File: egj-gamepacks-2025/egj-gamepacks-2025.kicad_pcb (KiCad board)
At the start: 2 copper layers, 52.3 x 64 mm, 81 parts, among them J1 USB_B_Micro, J2 Conn_01x03_Pin, J5 GameBoy_GamePak_AGB-002, SW1 SW_Push, SW2 SW_Push, U1 W25Q128JVS, U10 SP3012-06UTG, U11 VL6180XV0NR_1, U12 TXS0108EPW, U13 LD1117S18TR_SOT223, U14 BNO055, U15 SP3012-06UTG, U2 DNF, U3 NCP1117-3.3_SOT223, U4 RP2350_80QFN, U5 USBLC6-2P6, U6 SP3012-06UTG, U7 SP3012-06UTG, U8 SP3012-06UTG, U9 SP3012-06UTG, Y1 ABM8-272-T3

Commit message: UPDATE: sync local schematic and board work
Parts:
- removed C23: 100u, Capacitor_SMD:C_0805_2012Metric
- removed D1: BAT54CW, Package_TO_SOT_SMD:SOT-323_SC-70
- removed J2: Conn_01x03_Pin, Connector_PinHeader_2.54mm:PinHeader_1x03_P2.54mm_Horizontal
- removed U15: SP3012-06UTG, Package_DFN_QFN:DFN-14_1.35x3.5mm_P0.5mm
- added J3: SM03B-SRSS-TB, Connector_JST:JST_SH_SM03B-SRSS-TB_1x03-1MP_P1.00mm_Horizontal, F.Cu at (251.0, 109.0)
- added TP1: TestPoint, TestPoint:TestPoint_Keystone_5015_Micro_Mini, F.Cu at (261.0, 77.0)
- added TP2: TestPoint, TestPoint:TestPoint_Keystone_5015_Micro_Mini, F.Cu at (254.0, 75.0)
- added TP8: TestPoint, TestPoint:TestPoint_Keystone_5015_Micro_Mini, F.Cu at (246.0, 85.0)
- U13: value LD1117S18TR_SOT223 -> AP7361C-28E
- moved C9 140.2 mm to (273.0, 87.0), turned to 0 degrees
- moved C11 139.9 mm to (273.0, 91.0), turned to 0 degrees
- moved C8 139.9 mm to (273.0, 92.0), turned to 0 degrees
- moved R4 139.5 mm to (263.0, 93.0), turned to 0 degrees
- moved R19 133.6 mm to (273.0, 89.0), turned to 180 degrees
- moved R5 132.5 mm to (256.0, 106.0), turned to 0 degrees
- moved U1 131.5 mm to (256.0, 95.0)
- moved U2 131.5 mm to (256.0, 102.0)
- moved C12 129.8 mm to (263.0, 95.0), turned to 0 degrees
- moved R2 129.0 mm to (249.0, 105.0)
- moved SW1 128.6 mm to (244.0, 112.0)
- moved C3 127.8 mm to (248.0, 66.0)
- moved L1 127.4 mm to (263.0, 100.0)
- moved R10 126.7 mm to (273.0, 85.0), turned to 0 degrees
- moved U12 125.5 mm to (269.0, 97.0), turned to 180 degrees
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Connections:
- net /RP2350/+1V1 renamed +1V1
- C24 pad 1: +1V8 -> +2V8
- C26 pad 1: +1V8 -> +2V8
- C28 pad 1: +1V8 -> +2V8
- C29 pad 1: +1V8 -> +2V8
- C6 pad 1: +3V3_USB -> +3V3
- R10 pad 1: /Power/USB.USB_D_C+ -> /RP2350/USB_D+
- R11 pad 1: /Power/USB.USB_D_C- -> /RP2350/USB_D-
- R13 pad 1: +1V8 -> +2V8
- R14 pad 1: +1V8 -> +2V8
- R17 pad 1: +1V8 -> +2V8
- R18 pad 1: +1V8 -> +2V8
- U10 pad 1: /GBA_Connector/GBA_ADD13 -> unconnected-(U10-Pad1)
- U10 pad 11: /GBA_Connector/GBA_DATA0 -> /GBA_Connector/GBA_SIG.N_CS
- U10 pad 12: /GBA_Connector/GBA_ADD15 -> /GBA_Connector/GBA_SIG.N_RD
- U10 pad 13: /GBA_Connector/GBA_ADD14 -> /GBA_Connector/GBA_SIG.N_WR
- U10 pad 14: /GBA_Connector/GBA_ADD13 -> /GBA_Connector/GBA_SIG.PHI
- U10 pad 2: /GBA_Connector/GBA_ADD14 -> unconnected-(U10-Pad2)
- U10 pad 3: /GBA_Connector/GBA_ADD15 -> unconnected-(U10-Pad3)
- U10 pad 4: /GBA_Connector/GBA_DATA0 -> unconnected-(U10-Pad4)
- U10 pad 5: GND -> unconnected-(U10-Pad5)
- U10 pad 6: /GBA_Connector/GBA_DATA1 -> unconnected-(U10-Pad6)
- U10 pad 7: /GBA_Connector/GBA_DATA2 -> unconnected-(U10-Pad7)
- U10 pad 8: /GBA_Connector/GBA_DATA2 -> /GBA_Connector/GBA_SIG.IRQ
- U10 pad 9: /GBA_Connector/GBA_DATA1 -> /GBA_Connector/GBA_SIG.N_CS2
- U11 pad 10: +1V8 -> +2V8
- U11 pad 8: +1V8 -> +2V8
- U12 pad 2: +1V8 -> +2V8
- U13 pad 1: GND -> +3V3
- U13 pad 2: +1V8 -> GND
- U13 pad 3: +3V3 -> +2V8
- U3 pad 2: +3V3_USB -> +3V3
- U4 pad 1: /GBA_Connector/GBA_ADD0 -> /GBA_Connector/GBA_DATA4
- U4 pad 11: /GBA_Connector/GBA_ADD8 -> /GBA_Connector/GBA_ADD4
- U4 pad 12: /GBA_Connector/GBA_ADD9 -> /GBA_Connector/GBA_ADD5
- U4 pad 13: /GBA_Connector/GBA_ADD10 -> /GBA_Connector/GBA_ADD6
- U4 pad 14: /GBA_Connector/GBA_ADD11 -> /GBA_Connector/GBA_ADD7
- U4 pad 16: /GBA_Connector/GBA_ADD12 -> /GBA_Connector/GBA_ADD8
- U4 pad 17: /GBA_Connector/GBA_ADD13 -> /GBA_Connector/GBA_ADD9
- U4 pad 18: /GBA_Connector/GBA_ADD14 -> /GBA_Connector/GBA_ADD10
- U4 pad 19: /GBA_Connector/GBA_ADD15 -> /GBA_Connector/GBA_ADD11
- U4 pad 2: /GBA_Connector/GBA_ADD1 -> /GBA_Connector/GBA_DATA5
- U4 pad 20: /GBA_Connector/GBA_DATA0 -> /GBA_Connector/GBA_ADD12
- U4 pad 21: /GBA_Connector/GBA_DATA1 -> /GBA_Connector/GBA_ADD13
- U4 pad 22: /GBA_Connector/GBA_DATA2 -> /GBA_Connector/GBA_ADD14
- U4 pad 23: /GBA_Connector/GBA_DATA3 -> /GBA_Connector/GBA_ADD15
- U4 pad 25: /GBA_Connector/GBA_DATA4 -> /GBA_Connector/GBA_SIG.PHI
- U4 pad 26: /GBA_Connector/GBA_DATA5 -> /GBA_Connector/GBA_SIG.N_WR
- U4 pad 27: /GBA_Connector/GBA_DATA6 -> /GBA_Connector/GBA_SIG.N_RD
- U4 pad 28: /GBA_Connector/GBA_DATA7 -> /GBA_Connector/GBA_SIG.N_CS
- U4 pad 3: /GBA_Connector/GBA_ADD2 -> /GBA_Connector/GBA_DATA6
- U4 pad 4: /GBA_Connector/GBA_ADD3 -> /GBA_Connector/GBA_DATA7
- U4 pad 58: +3V3_USB -> unconnected-(U4-GPIO47_ADC7-Pad58)
- U4 pad 6: /GBA_Connector/GBA_ADD4 -> /GBA_Connector/GBA_ADD0
- U4 pad 7: /GBA_Connector/GBA_ADD5 -> /GBA_Connector/GBA_ADD1
- U4 pad 77: /GBA_Connector/GBA_SIG.PHI -> /GBA_Connector/GBA_DATA0
- U4 pad 78: /GBA_Connector/GBA_SIG.N_WR -> /GBA_Connector/GBA_DATA1
- U4 pad 79: /GBA_Connector/GBA_SIG.N_RD -> /GBA_Connector/GBA_DATA2
- U4 pad 8: /GBA_Connector/GBA_ADD6 -> /GBA_Connector/GBA_ADD2
- U4 pad 80: /GBA_Connector/GBA_SIG.N_CS -> /GBA_Connector/GBA_DATA3
- U4 pad 9: /GBA_Connector/GBA_ADD7 -> /GBA_Connector/GBA_ADD3
- U5 pad 2: unconnected-(U5-GND-Pad2) -> GND
- U5 pad 4: /Power/USB.USB_D_C- -> /RP2350/USB_D-
- U5 pad 5: GND -> VBUS
- U5 pad 6: /Power/USB.USB_D_C+ -> /RP2350/USB_D+
- U6 pad 1: /GBA_Connector/GBA_DATA3 -> unconnected-(U6-Pad1)
- U6 pad 11: /GBA_Connector/GBA_DATA6 -> /GBA_Connector/GBA_DATA3
- U6 pad 12: /GBA_Connector/GBA_DATA5 -> /GBA_Connector/GBA_DATA2
- U6 pad 13: /GBA_Connector/GBA_DATA4 -> /GBA_Connector/GBA_DATA1
- U6 pad 14: /GBA_Connector/GBA_DATA3 -> /GBA_Connector/GBA_DATA0
- U6 pad 2: /GBA_Connector/GBA_DATA4 -> unconnected-(U6-Pad2)
- U6 pad 3: /GBA_Connector/GBA_DATA5 -> unconnected-(U6-Pad3)
- U6 pad 4: /GBA_Connector/GBA_DATA6 -> unconnected-(U6-Pad4)
- U6 pad 5: GND -> unconnected-(U6-Pad5)
- U6 pad 6: /GBA_Connector/GBA_DATA7 -> unconnected-(U6-Pad6)
- U6 pad 7: /GBA_Connector/GBA_SIG.N_CS2 -> unconnected-(U6-Pad7)
- U6 pad 8: /GBA_Connector/GBA_SIG.N_CS2 -> /GBA_Connector/GBA_DATA5
- U6 pad 9: /GBA_Connector/GBA_DATA7 -> /GBA_Connector/GBA_DATA4
- U7 pad 1: /GBA_Connector/GBA_SIG.PHI -> unconnected-(U7-Pad1)
- U7 pad 11: /GBA_Connector/GBA_SIG.N_CS -> /GBA_Connector/GBA_ADD1
- U7 pad 12: /GBA_Connector/GBA_SIG.N_RD -> /GBA_Connector/GBA_ADD0
- U7 pad 13: /GBA_Connector/GBA_SIG.N_WR -> /GBA_Connector/GBA_DATA7
- U7 pad 14: /GBA_Connector/GBA_SIG.PHI -> /GBA_Connector/GBA_DATA6
- U7 pad 2: /GBA_Connector/GBA_SIG.N_WR -> unconnected-(U7-Pad2)
- U7 pad 3: /GBA_Connector/GBA_SIG.N_RD -> unconnected-(U7-Pad3)
- U7 pad 4: /GBA_Connector/GBA_SIG.N_CS -> unconnected-(U7-Pad4)
- U7 pad 5: GND -> unconnected-(U7-Pad5)
- U7 pad 6: /GBA_Connector/GBA_ADD0 -> unconnected-(U7-Pad6)
- U7 pad 7: /GBA_Connector/GBA_ADD1 -> unconnected-(U7-Pad7)
- U7 pad 8: /GBA_Connector/GBA_ADD1 -> /GBA_Connector/GBA_ADD3
- U7 pad 9: /GBA_Connector/GBA_ADD0 -> /GBA_Connector/GBA_ADD2
- U8 pad 1: /GBA_Connector/GBA_ADD2 -> unconnected-(U8-Pad1)
- U8 pad 11: /GBA_Connector/GBA_ADD4 -> /GBA_Connector/GBA_ADD7
- U8 pad 12: /GBA_Connector/GBA_ADD3 -> /GBA_Connector/GBA_ADD6
- U8 pad 13: /GBA_Connector/GBA_ADD2 -> /GBA_Connector/GBA_ADD5
- U8 pad 14: /GBA_Connector/GBA_ADD2 -> /GBA_Connector/GBA_ADD4
- U8 pad 2: /GBA_Connector/GBA_ADD2 -> unconnected-(U8-Pad2)
- U8 pad 3: /GBA_Connector/GBA_ADD3 -> unconnected-(U8-Pad3)
- U8 pad 4: /GBA_Connector/GBA_ADD4 -> unconnected-(U8-Pad4)
- U8 pad 5: GND -> unconnected-(U8-Pad5)
- U8 pad 6: /GBA_Connector/GBA_ADD5 -> unconnected-(U8-Pad6)
- U8 pad 7: /GBA_Connector/GBA_ADD6 -> unconnected-(U8-Pad7)
- U8 pad 8: /GBA_Connector/GBA_ADD6 -> /GBA_Connector/GBA_ADD9
- U8 pad 9: /GBA_Connector/GBA_ADD5 -> /GBA_Connector/GBA_ADD8
- U9 pad 1: /GBA_Connector/GBA_ADD7 -> unconnected-(U9-Pad1)
- U9 pad 11: /GBA_Connector/GBA_ADD10 -> /GBA_Connector/GBA_ADD13
- U9 pad 12: /GBA_Connector/GBA_ADD9 -> /GBA_Connector/GBA_ADD12
- U9 pad 13: /GBA_Connector/GBA_ADD8 -> /GBA_Connector/GBA_ADD11
- U9 pad 14: /GBA_Connector/GBA_ADD7 -> /GBA_Connector/GBA_ADD10
- U9 pad 2: /GBA_Connector/GBA_ADD8 -> unconnected-(U9-Pad2)
- U9 pad 3: /GBA_Connector/GBA_ADD9 -> unconnected-(U9-Pad3)
- U9 pad 4: /GBA_Connector/GBA_ADD10 -> unconnected-(U9-Pad4)
- U9 pad 5: GND -> unconnected-(U9-Pad5)
- U9 pad 6: /GBA_Connector/GBA_ADD11 -> unconnected-(U9-Pad6)
- U9 pad 7: /GBA_Connector/GBA_ADD12 -> unconnected-(U9-Pad7)
- U9 pad 8: /GBA_Connector/GBA_ADD12 -> /GBA_Connector/GBA_ADD15
- U9 pad 9: /GBA_Connector/GBA_ADD11 -> /GBA_Connector/GBA_ADD14
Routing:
- net +3V3: track 55.3 -> 0.00 mm
- net /GBA_Connector/GBA_ADD0: track 0.00 -> 32.9 mm
- net /GBA_Connector/GBA_ADD1: track 0.00 -> 31.3 mm
- net /GBA_Connector/GBA_ADD2: track 0.00 -> 29.8 mm
- net /GBA_Connector/GBA_ADD3: track 0.00 -> 28.3 mm
- net /GBA_Connector/GBA_ADD4: track 0.00 -> 26.7 mm
- net /GBA_Connector/GBA_ADD5: track 0.00 -> 25.2 mm
- net /GBA_Connector/GBA_ADD6: track 0.00 -> 23.6 mm
- net /GBA_Connector/GBA_ADD7: track 0.00 -> 22.1 mm
- net VBUS: track 21.7 -> 0.00 mm
- net /GBA_Connector/GBA_ADD8: track 0.00 -> 20.6 mm
- net /GBA_Connector/GBA_ADD9: track 0.00 -> 19.0 mm
- net +3V3_USB: track 17.0 -> 0.00 mm
- net +1V8: track 8.68 -> 0.00 mm
- net +3V3_GBA: track 1.87 -> 0.00 mm
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- removed copper zone on B.Cu, net (none)
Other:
- outline, holes or cut-outs redrawn

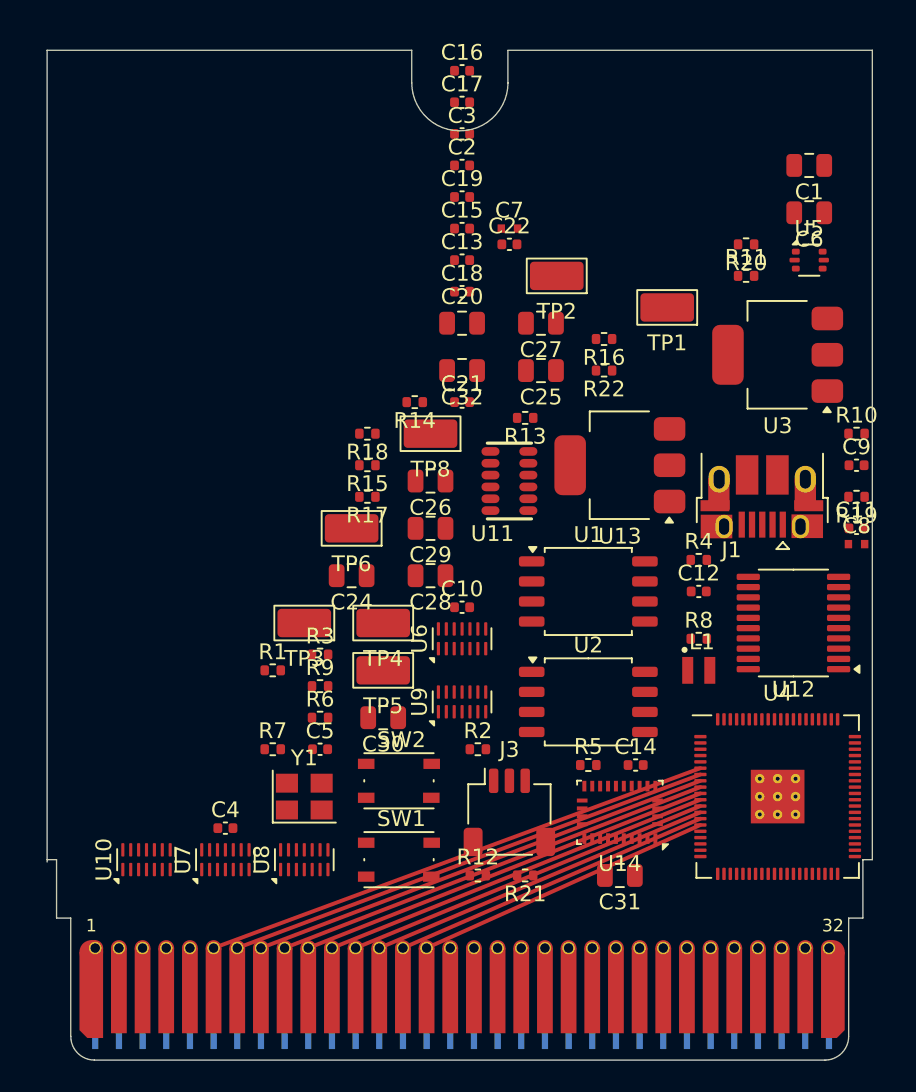
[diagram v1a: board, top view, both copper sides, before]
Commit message: ADD: board placement and full two-layer routing with JLCPCB design rules
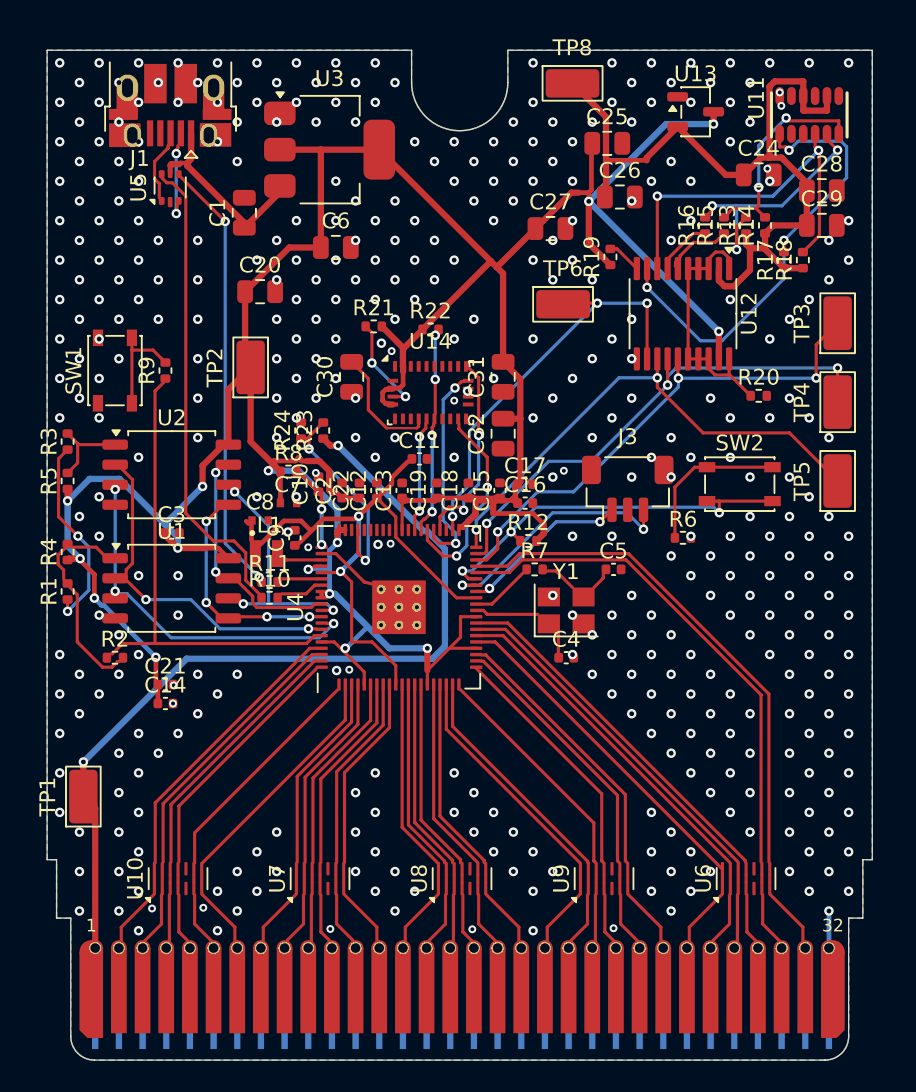
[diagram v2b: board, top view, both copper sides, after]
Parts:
- added R23: 100k, Resistor_SMD:R_0402_1005Metric, F.Cu at (239.2, 84.8)
- added R24: 100k, Resistor_SMD:R_0402_1005Metric, F.Cu at (237.8, 84.8)
- J3: value SM03B-SRSS-TB -> BM03B-SRSS-TB; footprint Connector_JST:JST_SH_SM03B-SRSS-TB_1x03-1MP_P1.00mm_Horizontal -> Connector_JST:JST_SH_BM03B-SRSS-TB_1x03-1MP_P1.00mm_Vertical
- SW1, SW2: value SW_Push -> PTS810SJG250SMTRLFS; footprint Button_Switch_SMD:SW_Push_1P1T_NO_Vertical_Wuerth_434133025816 -> Button_Switch_SMD:SW_SPST_PTS810
- U1: value W25Q128JVS -> W25Q128JVSIQ
- U10, U6, U7, U8, U9: value SP3012-06UTG -> TPD6E05U06RVZR
- U11: value VL6180XV0NR_1 -> VL6180V1NR/1
- U13: value AP7361C-28E -> XC6206P282MR; footprint Package_TO_SOT_SMD:SOT-223-3_TabPin2 -> Package_TO_SOT_SMD:SOT-23-3
- moved TP1 48.3 mm to (224.0, 108.0), turned to 90 degrees
- moved J1 45.0 mm to (229.5, 64.2)
- moved U5 40.8 mm to (229.5, 69.4), turned to 90 degrees
- moved R4 40.0 mm to (223.0, 92.5), turned to 90 degrees
- moved TP3 38.8 mm to (271.8, 78.0), turned to 90 degrees
- moved R10 38.6 mm to (235.8, 95.4)
- moved C8 37.8 mm to (235.2, 90.5)
- moved R5 37.6 mm to (223.0, 88.0), turned to 90 degrees
- moved C24 36.2 mm to (266.8, 68.6), turned to 0 degrees
- moved R21 36.1 mm to (242.4, 78.2), turned to 0 degrees
- moved C1 35.9 mm to (234.2, 71.0), turned to 90 degrees
- moved C9 35.9 mm to (237.4, 91.6), turned to 90 degrees
- moved R11 35.9 mm to (235.8, 94.4)
- moved SW1 35.8 mm to (226.0, 81.0), turned to 90 degrees
- moved C28 34.8 mm to (270.8, 69.6), turned to 0 degrees
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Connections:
- R22 pad 1: /RP2350/BNO055_UART.RESET -> +3V3
- R22 pad 2: +3V3 -> /RP2350/BNO055_UART.RESET
- U10 pad 1: unconnected-(U10-Pad1) -> /GBA_Connector/GBA_SIG.PHI
- U10 pad 2: unconnected-(U10-Pad2) -> /GBA_Connector/GBA_SIG.N_WR
- U10 pad 3: unconnected-(U10-Pad3) -> /GBA_Connector/GBA_SIG.N_RD
- U10 pad 4: unconnected-(U10-Pad4) -> /GBA_Connector/GBA_SIG.N_CS
- U10 pad 5: unconnected-(U10-Pad5) -> GND
- U10 pad 6: unconnected-(U10-Pad6) -> /GBA_Connector/GBA_ADD0
- U10 pad 7: unconnected-(U10-Pad7) -> /GBA_Connector/GBA_ADD1
- U10 pad 8: /GBA_Connector/GBA_SIG.IRQ -> /GBA_Connector/GBA_ADD1
- U10 pad 9: /GBA_Connector/GBA_SIG.N_CS2 -> /GBA_Connector/GBA_ADD0
- U13 pad 1: +3V3 -> GND
- U13 pad 2: GND -> +2V8
- U13 pad 3: +2V8 -> +3V3
- U14 pad 11: +3V3 -> /RP2350/BNO055_UART.RESET
- U4 pad 1: /GBA_Connector/GBA_DATA4 -> /GBA_Connector/GBA_ADD0
- U4 pad 11: /GBA_Connector/GBA_ADD4 -> /GBA_Connector/GBA_ADD8
- U4 pad 12: /GBA_Connector/GBA_ADD5 -> /GBA_Connector/GBA_ADD9
- U4 pad 13: /GBA_Connector/GBA_ADD6 -> /GBA_Connector/GBA_ADD10
- U4 pad 14: /GBA_Connector/GBA_ADD7 -> /GBA_Connector/GBA_ADD11
- U4 pad 16: /GBA_Connector/GBA_ADD8 -> /GBA_Connector/GBA_ADD12
- U4 pad 17: /GBA_Connector/GBA_ADD9 -> /GBA_Connector/GBA_ADD13
- U4 pad 18: /GBA_Connector/GBA_ADD10 -> /GBA_Connector/GBA_ADD14
- U4 pad 19: /GBA_Connector/GBA_ADD11 -> /GBA_Connector/GBA_ADD15
- U4 pad 2: /GBA_Connector/GBA_DATA5 -> /GBA_Connector/GBA_ADD1
- U4 pad 20: /GBA_Connector/GBA_ADD12 -> /GBA_Connector/GBA_DATA0
- U4 pad 21: /GBA_Connector/GBA_ADD13 -> /GBA_Connector/GBA_DATA1
- U4 pad 22: /GBA_Connector/GBA_ADD14 -> /GBA_Connector/GBA_DATA2
- U4 pad 23: /GBA_Connector/GBA_ADD15 -> /GBA_Connector/GBA_DATA3
- U4 pad 25: /GBA_Connector/GBA_SIG.PHI -> /GBA_Connector/GBA_DATA4
- U4 pad 26: /GBA_Connector/GBA_SIG.N_WR -> /GBA_Connector/GBA_DATA5
- U4 pad 27: /GBA_Connector/GBA_SIG.N_RD -> /GBA_Connector/GBA_DATA6
- U4 pad 28: /GBA_Connector/GBA_SIG.N_CS -> /GBA_Connector/GBA_DATA7
- U4 pad 3: /GBA_Connector/GBA_DATA6 -> /GBA_Connector/GBA_ADD2
- U4 pad 4: /GBA_Connector/GBA_DATA7 -> /GBA_Connector/GBA_ADD3
- U4 pad 57: +3V3_GBA -> Net-(U4-GPIO46_ADC6)
- U4 pad 6: /GBA_Connector/GBA_ADD0 -> /GBA_Connector/GBA_ADD4
- U4 pad 7: /GBA_Connector/GBA_ADD1 -> /GBA_Connector/GBA_ADD5
- U4 pad 77: /GBA_Connector/GBA_DATA0 -> /GBA_Connector/GBA_SIG.PHI
- U4 pad 78: /GBA_Connector/GBA_DATA1 -> /GBA_Connector/GBA_SIG.N_WR
- U4 pad 79: /GBA_Connector/GBA_DATA2 -> /GBA_Connector/GBA_SIG.N_RD
- U4 pad 8: /GBA_Connector/GBA_ADD2 -> /GBA_Connector/GBA_ADD6
- U4 pad 80: /GBA_Connector/GBA_DATA3 -> /GBA_Connector/GBA_SIG.N_CS
- U4 pad 9: /GBA_Connector/GBA_ADD3 -> /GBA_Connector/GBA_ADD7
- U6 pad 1: unconnected-(U6-Pad1) -> /GBA_Connector/GBA_DATA4
- U6 pad 11: /GBA_Connector/GBA_DATA3 -> /GBA_Connector/GBA_DATA7
- U6 pad 12: /GBA_Connector/GBA_DATA2 -> /GBA_Connector/GBA_DATA6
- U6 pad 13: /GBA_Connector/GBA_DATA1 -> /GBA_Connector/GBA_DATA5
- U6 pad 14: /GBA_Connector/GBA_DATA0 -> /GBA_Connector/GBA_DATA4
- U6 pad 2: unconnected-(U6-Pad2) -> /GBA_Connector/GBA_DATA5
- U6 pad 3: unconnected-(U6-Pad3) -> /GBA_Connector/GBA_DATA6
- U6 pad 4: unconnected-(U6-Pad4) -> /GBA_Connector/GBA_DATA7
- U6 pad 5: unconnected-(U6-Pad5) -> GND
- U6 pad 6: unconnected-(U6-Pad6) -> /GBA_Connector/GBA_SIG.N_CS2
- U6 pad 7: unconnected-(U6-Pad7) -> /GBA_Connector/GBA_SIG.IRQ
- U6 pad 8: /GBA_Connector/GBA_DATA5 -> /GBA_Connector/GBA_SIG.IRQ
- U6 pad 9: /GBA_Connector/GBA_DATA4 -> /GBA_Connector/GBA_SIG.N_CS2
- U7 pad 1: unconnected-(U7-Pad1) -> /GBA_Connector/GBA_ADD2
- U7 pad 11: /GBA_Connector/GBA_ADD1 -> /GBA_Connector/GBA_ADD5
- U7 pad 12: /GBA_Connector/GBA_ADD0 -> /GBA_Connector/GBA_ADD4
- U7 pad 13: /GBA_Connector/GBA_DATA7 -> /GBA_Connector/GBA_ADD3
- U7 pad 14: /GBA_Connector/GBA_DATA6 -> /GBA_Connector/GBA_ADD2
- U7 pad 2: unconnected-(U7-Pad2) -> /GBA_Connector/GBA_ADD3
- U7 pad 3: unconnected-(U7-Pad3) -> /GBA_Connector/GBA_ADD4
- U7 pad 4: unconnected-(U7-Pad4) -> /GBA_Connector/GBA_ADD5
- U7 pad 5: unconnected-(U7-Pad5) -> GND
- U7 pad 6: unconnected-(U7-Pad6) -> /GBA_Connector/GBA_ADD6
- U7 pad 7: unconnected-(U7-Pad7) -> /GBA_Connector/GBA_ADD7
- U7 pad 8: /GBA_Connector/GBA_ADD3 -> /GBA_Connector/GBA_ADD7
- U7 pad 9: /GBA_Connector/GBA_ADD2 -> /GBA_Connector/GBA_ADD6
- U8 pad 1: unconnected-(U8-Pad1) -> /GBA_Connector/GBA_ADD8
- U8 pad 11: /GBA_Connector/GBA_ADD7 -> /GBA_Connector/GBA_ADD11
- U8 pad 12: /GBA_Connector/GBA_ADD6 -> /GBA_Connector/GBA_ADD10
- U8 pad 13: /GBA_Connector/GBA_ADD5 -> /GBA_Connector/GBA_ADD9
- U8 pad 14: /GBA_Connector/GBA_ADD4 -> /GBA_Connector/GBA_ADD8
- U8 pad 2: unconnected-(U8-Pad2) -> /GBA_Connector/GBA_ADD9
- U8 pad 3: unconnected-(U8-Pad3) -> /GBA_Connector/GBA_ADD10
- U8 pad 4: unconnected-(U8-Pad4) -> /GBA_Connector/GBA_ADD11
- U8 pad 5: unconnected-(U8-Pad5) -> GND
- U8 pad 6: unconnected-(U8-Pad6) -> /GBA_Connector/GBA_ADD12
- U8 pad 7: unconnected-(U8-Pad7) -> /GBA_Connector/GBA_ADD13
- U8 pad 8: /GBA_Connector/GBA_ADD9 -> /GBA_Connector/GBA_ADD13
- U8 pad 9: /GBA_Connector/GBA_ADD8 -> /GBA_Connector/GBA_ADD12
- U9 pad 1: unconnected-(U9-Pad1) -> /GBA_Connector/GBA_ADD14
- U9 pad 11: /GBA_Connector/GBA_ADD13 -> /GBA_Connector/GBA_DATA1
- U9 pad 12: /GBA_Connector/GBA_ADD12 -> /GBA_Connector/GBA_DATA0
- U9 pad 13: /GBA_Connector/GBA_ADD11 -> /GBA_Connector/GBA_ADD15
- U9 pad 14: /GBA_Connector/GBA_ADD10 -> /GBA_Connector/GBA_ADD14
- U9 pad 2: unconnected-(U9-Pad2) -> /GBA_Connector/GBA_ADD15
- U9 pad 3: unconnected-(U9-Pad3) -> /GBA_Connector/GBA_DATA0
- U9 pad 4: unconnected-(U9-Pad4) -> /GBA_Connector/GBA_DATA1
- U9 pad 5: unconnected-(U9-Pad5) -> GND
- U9 pad 6: unconnected-(U9-Pad6) -> /GBA_Connector/GBA_DATA2
- U9 pad 7: unconnected-(U9-Pad7) -> /GBA_Connector/GBA_DATA3
- U9 pad 8: /GBA_Connector/GBA_ADD15 -> /GBA_Connector/GBA_DATA3
- U9 pad 9: /GBA_Connector/GBA_ADD14 -> /GBA_Connector/GBA_DATA2
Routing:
- net +3V3: track 0.00 -> 223.0 mm, vias 0 -> 15
- net +3V3_GBA: track 0.00 -> 54.8 mm, vias 0 -> 2
- net +2V8: track 0.00 -> 51.4 mm
- net /GBA_Connector/GBA_SIG.IRQ: track 0.00 -> 37.1 mm
- net +1V1: track 0.00 -> 36.2 mm, vias 0 -> 2
- net /GBA_Connector/GBA_SIG.N_CS2: track 0.00 -> 36.0 mm
- net /RP2350/VL6180XV0NR_I2C.SCL: track 0.00 -> 32.9 mm, vias 0 -> 3
- net /RP2350/VL6180XV0NR_I2C.GPIO0: track 0.00 -> 32.6 mm, vias 0 -> 2
- net /RP2350/VL6180XV0NR_I2C.SDA: track 0.00 -> 32.5 mm, vias 0 -> 3
- net /RP2350/QSPI_SS: track 0.00 -> 30.2 mm
- net /RP2350/USB_D+: track 0.00 -> 29.9 mm
- net /sensor_part/GPIO1_18: track 0.00 -> 29.2 mm, vias 0 -> 3
- net /RP2350/USB_D-: track 0.00 -> 27.4 mm, vias 0 -> 2
- net /RP2350/VL6180XV0NR_I2C.GPIO1: track 0.00 -> 27.1 mm, vias 0 -> 3
- net /GBA_Connector/GBA_DATA7: track 0.00 -> 26.6 mm
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- added copper zone on B.Cu, net GND
- added copper zone on F.Cu, net GND
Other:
- outline, holes or cut-outs redrawn
